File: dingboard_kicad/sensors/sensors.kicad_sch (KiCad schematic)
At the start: 49 parts, among them J1 Bus_PCI_Express_x1, J2 TYPE-C-31-M-04, J3 Conn_01x02, U2 RP2040, U3 TPS2121RUXR, U4 W25Q128JVP, U5 BMP388, U6 LMR51430 1.1k FPWM, U7 MCP25625-x-SS, U8 BNO055, X1 ABM8-272-T3

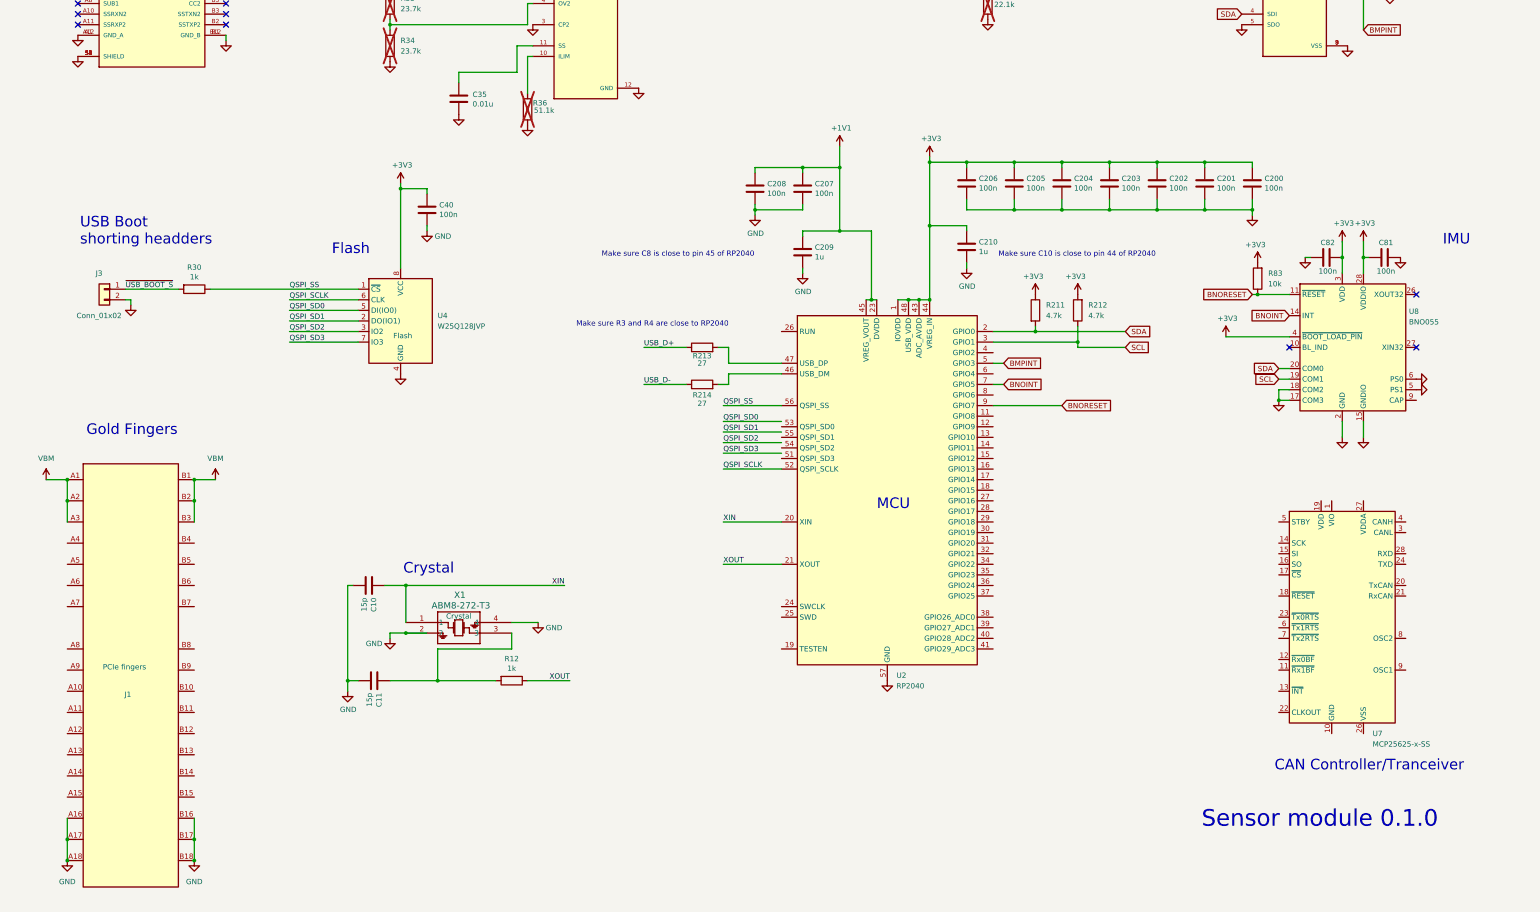
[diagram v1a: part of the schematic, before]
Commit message: update BNO055 schematic
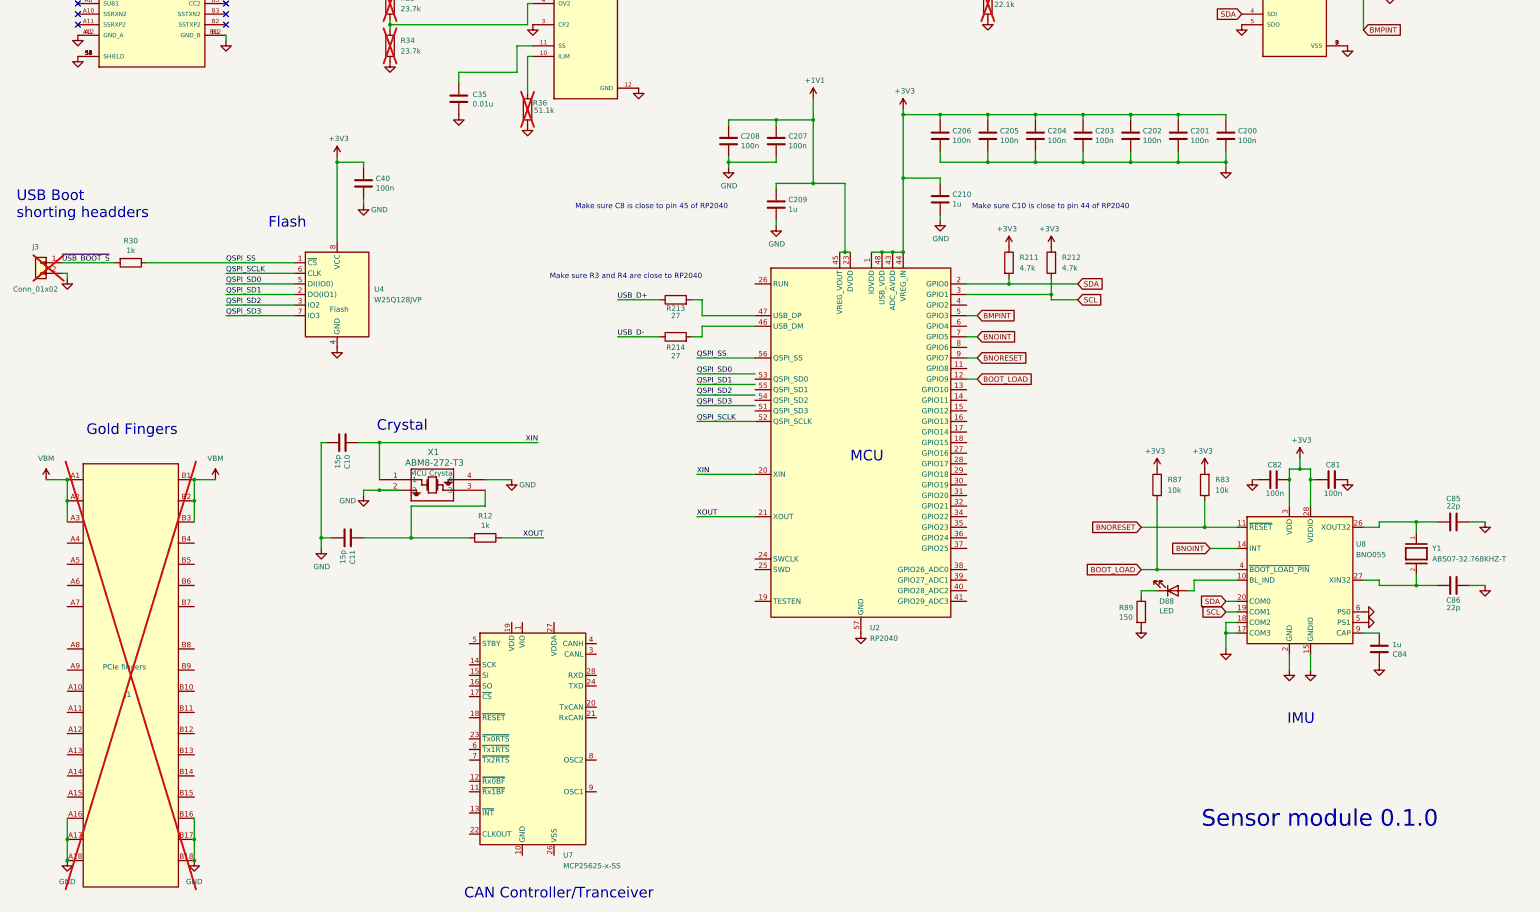
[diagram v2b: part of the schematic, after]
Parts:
- added C84: 1u, Capacitor_SMD:C_0402_1005Metric, symbol Device:C
- added C85, C86: 22p, Capacitor_SMD:C_0402_1005Metric, symbol Device:C
- added D88: LED, LED_SMD:LED_0603_1608Metric, symbol Device:LED
- added R87: 10k, Resistor_SMD:R_0402_1005Metric, symbol Device:R
- added R89: 150, Resistor_SMD:R_0603_1608Metric, symbol Device:R
- added Y1: ABS07-32.768KHZ-T, ABS07-32.768KHZ-T:XTAL_ABS07-32.768KHZ-T, symbol ABS07-32.768KHZ-T:ABS07-32.768KHZ-T
- C10, C11: JLC Link (none) -> https://jlcpcb.com/partdetail/1900-0402CG150J500NT/C1548; link https://jlcpcb.com/partdetail/1900-0402CG150J500NT/C1548 -> (none)
- C200, C201, C202, C203, C204, C205, C206, C207, C208, C40, C50, C51, C60, C81, C82: JLC Link (none) -> https://jlcpcb.com/partdetail/291005-CL05B104KB54PNC/C307331; link https://jlcpcb.com/partdetail/291005-CL05B104KB54PNC/C307331 -> (none)
- C209, C210: JLC Link (none) -> https://jlcpcb.com/partdetail/53938-CL05A105KA5NQNC/C52923; link https://jlcpcb.com/partdetail/53938-CL05A105KA5NQNC/C52923 -> (none)
- C30: JLC Link (none) -> https://jlcpcb.com/partdetail/15681-CL31A107MQHNNNE/C15008; link https://jlcpcb.com/partdetail/15681-CL31A107MQHNNNE/C15008 -> (none)
- C35: JLC Link (none) -> https://jlcpcb.com/partdetail/15869-CL05B103KB5NNNC/C15195; info 0.01uF Cap -> 10pF Cap; link https://jlcpcb.com/partdetail/15869-CL05B103KB5NNNC/C15195 -> (none)
- C63, C65: footprint 0603 -> Capacitor_SMD:C_0603_1608Metric; JLC Link (none) -> https://jlcpcb.com/partdetail/97651-CL10A106MA8NRNC/C96446; link https://jlcpcb.com/partdetail/97651-CL10A106MA8NRNC/C96446 -> (none)
- C64: JLC Link (none) -> https://jlcpcb.com/partdetail/13164-CL05A225MQ5NSNC/C12530; link https://jlcpcb.com/partdetail/13164-CL05A225MQ5NSNC/C12530 -> (none)
- J1, J3: JLC Link (none) -> n/a; link n/a -> (none); now not fitted
- J2: JLC Link (none) -> https://jlcpcb.com/partdetail/Korean_HropartsElec-TYPE_C_31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; link https://jlcpcb.com/partdetail/Korean_HropartsElec-TYPE_C_31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 -> (none)
- R12, R30: JLC Link (none) -> https://jlcpcb.com/partdetail/12256-0402WGF1001TCE/C11702; link https://jlcpcb.com/partdetail/12256-0402WGF1001TCE/C11702 -> (none)
- R211, R212: JLC Link (none) -> https://jlcpcb.com/partdetail/26643-0402WGF4701TCE/C25900; link https://jlcpcb.com/partdetail/26643-0402WGF4701TCE/C25900 -> (none)
- R213, R214: JLC Link (none) -> https://jlcpcb.com/partdetail/25933-0603WAF270JT5E/C25190; link https://jlcpcb.com/partdetail/25933-0603WAF270JT5E/C25190 -> (none)
- R31, R32, R33, R34: footprint 0603 -> Resistor_SMD:R_0603_1608Metric; Digikey Link (none) -> https://www.digikey.ca/en/products/detail/stackpole-electro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; link https://jlcpcb.com/partdetail/23639-0603WAF2372T5E/C22912 -> (none); price C$0.0013 -> $0.16
- R36: footprint 0603 -> Resistor_SMD:R_0603_1608Metric; Digikey Link (none) -> https://www.digikey.ca/en/products/detail/yageo/RC0603FR-07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; link https://jlcpcb.com/partdetail/23799-0603WAF5112T5E/C23072 -> (none); price C$0.0013 -> $0.16
- R61: JLC Link (none) -> https://jlcpcb.com/partdetail/26484-0402WGF1003TCE/C25741; link https://jlcpcb.com/partdetail/26484-0402WGF1003TCE/C25741 -> (none)
- R62: footprint 0603 -> Resistor_SMD:R_0603_1608Metric; Digikey Link (none) -> https://www.digikey.ca/en/products/detail/stackpole-electro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; link https://jlcpcb.com/partdetail/26704-0603WAF2212T5E/C25961 -> (none); price C$0.0013 -> $0.16
- R83: JLC Link (none) -> https://jlcpcb.com/partdetail/26487-0402WGF1002TCE/C25744; link https://jlcpcb.com/partdetail/26487-0402WGF1002TCE/C25744 -> (none)
- U2: JLC Link (none) -> https://jlcpcb.com/partdetail/RaspberryPi-RP2040/C2040; link https://jlcpcb.com/partdetail/RaspberryPi-RP2040/C2040 -> (none)
- U3: JLC Link (none) -> https://jlcpcb.com/partdetail/TexasInstruments-TPS2121RUXR/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; link https://jlcpcb.com/partdetail/TexasInstruments-TPS2121RUXR/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 -> (none)
- U4: JLC Link (none) -> https://jlcpcb.com/partdetail/WinbondElec-W25Q128JVPIQ/C190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; link https://jlcpcb.com/partdetail/WinbondElec-W25Q128JVPIQ/C190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 -> (none)
- U5: JLC Link (none) -> https://jlcpcb.com/partdetail/BoschSensortec-BMP388/C779278; info Altimeter -> BMP288; link https://jlcpcb.com/partdetail/BoschSensortec-BMP388/C779278 -> (none)
- U6: JLC Link (none) -> https://jlcpcb.com/partdetail/TexasInstruments-LMR51430YFDD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; link https://jlcpcb.com/partdetail/TexasInstruments-LMR51430YFDD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 -> (none)
- U7: JLC Link (none) -> https://jlcpcb.com/partdetail/MicrochipTech-MCP25625_ESS/C1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; link https://jlcpcb.com/partdetail/MicrochipTech-MCP25625_ESS/C1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 -> (none)
- U8: JLC Link (none) -> https://jlcpcb.com/partdetail/BoschSensortec-BNO055/C93216; info IMU -> BNO055; link https://jlcpcb.com/partdetail/BoschSensortec-BNO055/C93216 -> (none)
- X1: JLC Link (none) -> https://jlcpcb.com/partdetail/AbraconLlc-ABM8_272T3/C206257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; info Crystal -> MCU Crystal; link https://jlcpcb.com/partdetail/AbraconLlc-ABM8_272T3/C206257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 -> (none)
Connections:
- net +3V3: now also R87.2; no longer U8.4 (~{BOOT_LOAD_PIN})
- net GND: now also C84.1, C85.2, C86.1, R89.2
- net at U8.10 (BL_IND): now also D88.2 (A)
- net at U8.26 (XOUT32): now also C85.1, Y1.1
- net at U8.27 (XIN32): now also C86.2, Y1.2
- net at U8.9 (CAP): now also C84.2
- net BOOT_LOAD: now reaches U2.12 (GPIO9)
- net BOOT_LOAD: now also U8.4 (~{BOOT_LOAD_PIN}), R87.1
- new net: D88.1 (K), R89.1
- no-connect marks 15 -> 12
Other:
- moved on the sheet: C10, C11, C200, C201, C202, C203, C204, C205, C206, C207, C208, C209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

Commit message: add 5v buck-boost for CAN chip
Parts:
- removed U7: MCP25625-x-SS, Package_SO:SSOP-28_5.3x10.2mm_P0.65mm, symbol Interface_CAN_LIN:MCP25625-x-SS
- added C700: 10u, Capacitor_SMD:C_0402_1005Metric, symbol Device:C
- added C73: 100n, symbol Device:C
- added C74, C75, C76: 10uF, Capacitor_SMD:C_0402_1005Metric, symbol Device:C
- added C77, C78, C79: 22u, Capacitor_SMD:C_0402_1005Metric, symbol Device:C
- added L66: 2.2u, Inductor_SMD:L_0603_1608Metric, symbol Device:L
- added L70: 1.5u, Inductor_SMD:L_0603_1608Metric, symbol Device:L
- added R71: 10k, Resistor_SMD:R_0402_1005Metric, symbol Device:R
- added R72: 100k, Resistor_SMD:R_0402_1005Metric, symbol Device:R
- added U1: MCP25625T-E/ML, MCP25625:QFN28_6X6MC_MCH, symbol MCP25625:MCP25625T-E_ML
- added U7: TPS63070RNMR, TPS63070RNMR:VREG_TPS63070RNMR, symbol TPS63070RNMR:TPS63070RNMR
- C63, C65: value 10uF / 25v -> 10uF/25v
- R31, R33: Digikey Link https://www.digikey.ca/en/products/detail/stackpole-electro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 -> (none); LCSC Part # C22912 -> (none); basic? no -> (none); price $0.16 -> (none)
- R32, R34: value 23.7k -> 5k; Digikey Link https://www.digikey.ca/en/products/detail/stackpole-electro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 -> (none); LCSC Part # C22912 -> (none); basic? no -> (none); price $0.16 -> (none)
- U3: basic? (none) -> no
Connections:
- net +3.3V: now also L66.2; no longer C60.2, U6.2 (SW)
- net GND: now also C700.2, C73.2, C74.2, C75.2, C76.2, C77.2, C78.2, C79.2, U7.10 (PGND), U7.15 (VSEL), U7.4 (GND), U7.6 (FB2)
- net vpre: now also C74.1, C75.1, C76.1, R71.1, U7.12_13 (VIN)
- new net: C60.2, L66.1, U6.2 (SW)
- new net: R72.1, U7.2 (PG)
- new net: L70.1, U7.11 (L1)
- new net: L70.2, U7.9 (L2)
- new net: C73.1, U7.3 (VAUX)
- new net: R71.2, U7.1 (PS/SYNC), U7.14 (EN)
- new net +5V: C700.1, C77.1, C78.1, C79.1, R72.2, U7.5 (FB), U7.7_8 (VOUT)
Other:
- note added: "3.3v Regulator"
- note added: "5v Buck-Boost"
- note removed: "Regulator"
- moved on the sheet: C10, C11, C200, C201, C202, C203, C204, C205, C206, C207, C208, C209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
